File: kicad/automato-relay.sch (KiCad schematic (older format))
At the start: 51 parts, among them J1 TE-3-213598-4, J2 IEC-C14-FUSE, J3 TE-3-213598-4, J4 Screw_Terminal_01x05, J5 TE-3-213598-4, J6 TE-3-213598-4, J7 Screw_Terminal_01x05, J8 TE-3-213598-4, K1 G5LE-14, K2 G5LE-14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

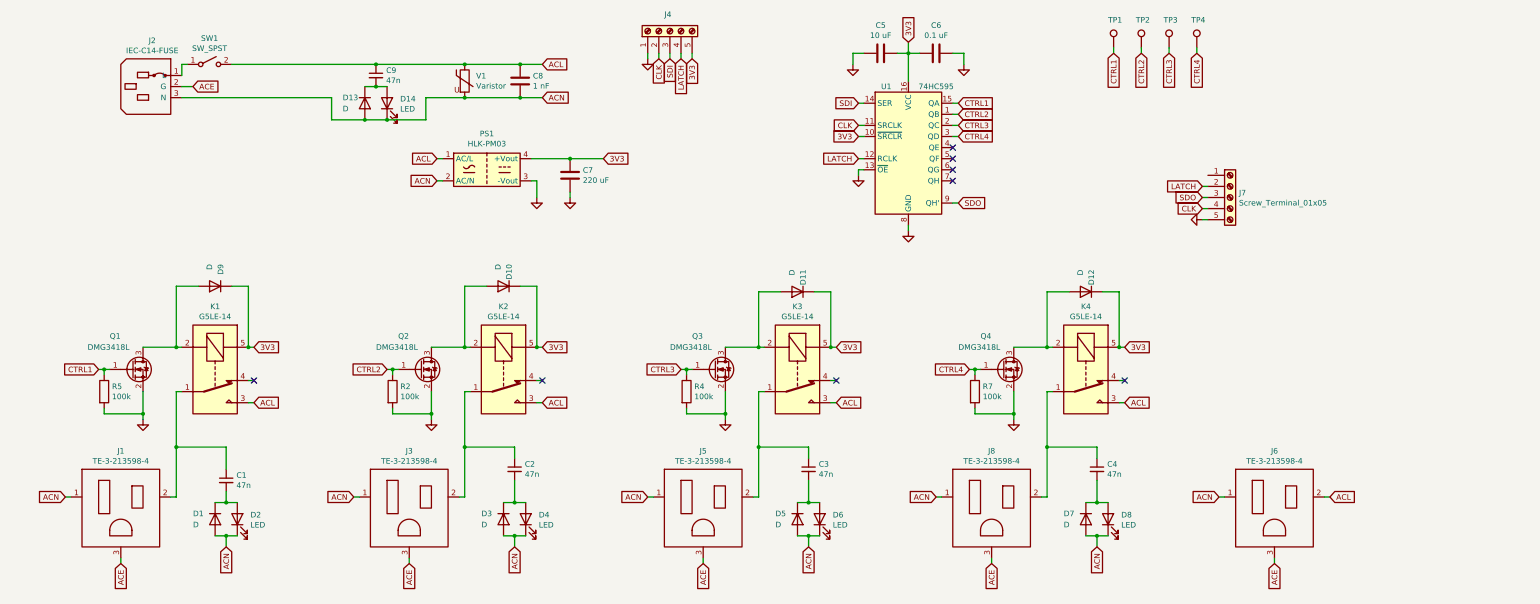
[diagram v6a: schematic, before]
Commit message: replaced 5-pin connectors with usb-c receptacles
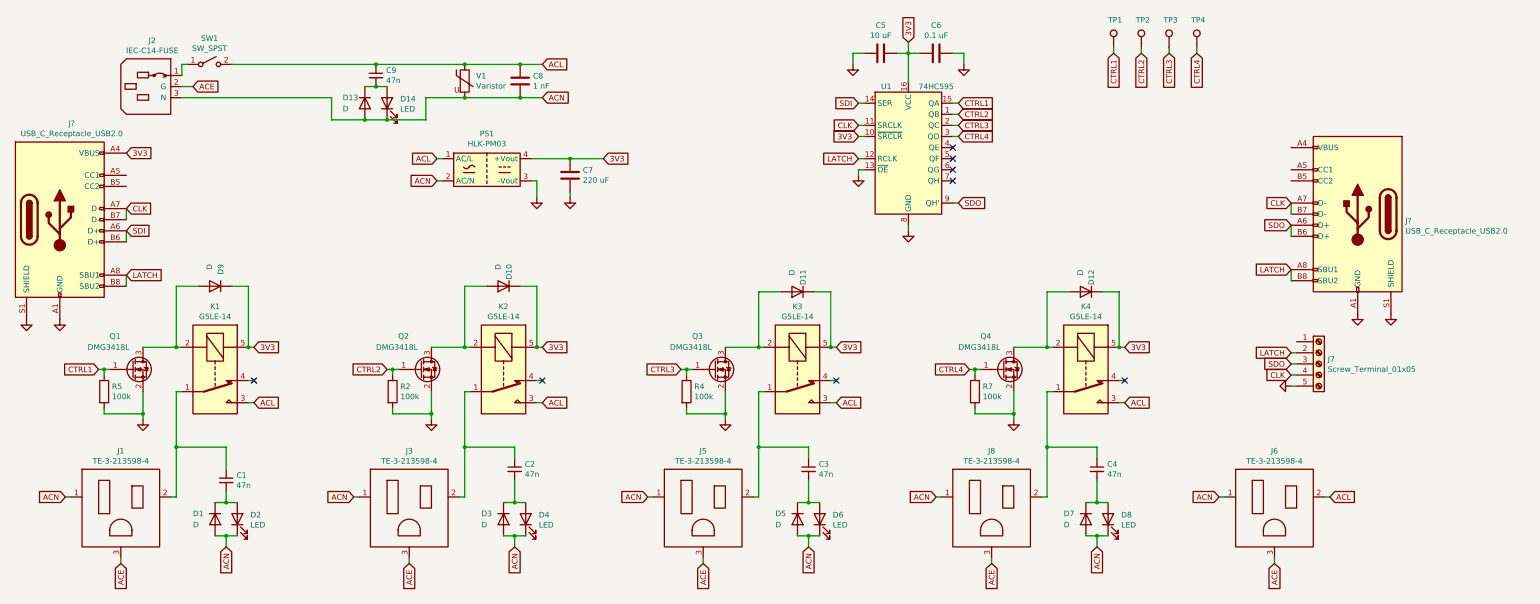
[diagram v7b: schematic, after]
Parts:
- removed J4: Screw_Terminal_01x05, automato-relay:PhoenixContact_1935190_1x5, symbol Connector:Screw_Terminal_01x05
- added J? (x2): USB_C_Receptacle_USB2.0, symbol Connector:USB_C_Receptacle_USB2.0
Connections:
- net 3V3: now also J?.A4 (VBUS), J?.A9 (VBUS), J?.B4 (VBUS), J?.B9 (VBUS)
- net CLK: now also J?.A7 (D-), J?.A7 (D-), J?.B7 (D-), J?.B7 (D-)
- net GND: now also J?.A1 (GND), J?.A1 (GND), J?.A12 (GND), J?.A12 (GND), J?.B1 (GND), J?.B1 (GND), J?.B12 (GND), J?.B12 (GND), J?.S1 (SHIELD), J?.S1 (SHIELD)
- net LATCH: now also J?.A8 (SBU1), J?.A8 (SBU1), J?.B8 (SBU2), J?.B8 (SBU2)
- net SDI: now also J?.A6 (D+), J?.B6 (D+)
- net SDO: now also J?.A6 (D+), J?.B6 (D+)
- new net: J?.A4 (VBUS), J?.A9 (VBUS), J?.B4 (VBUS), J?.B9 (VBUS)
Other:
- moved on the sheet: J7
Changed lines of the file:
@@
 	8300 2200 8350 2200
-$Comp
-L power:GND #PWR06
-U 1 1 601F84F8
-P 6400 1300
-F 0 "#PWR06" H 6400 1050 50  0001 C CNN
-F 1 "GND" H 6405 1127 50  0001 C CNN
-F 2 "" H 6400 1300 50  0001 C CNN
-F 3 "" H 6400 1300 50  0001 C CNN
-	1    6400 1300
-	1    0    0    -1
-$EndComp
-Wire Wire Line
-	6400 1250 6400 1300
-Wire Wire Line
-	6500 1250 6500 1300
-Wire Wire Line
-	6600 1250 6600 1300
-Wire Wire Line
-	6700 1250 6700 1300
 $Comp
 L power:GND #PWR012
 U 1 1 60208E2A
-P 11400 2750
-F 0 "#PWR012" H 11400 2500 50  0001 C CNN
-F 1 "GND" H 11405 2577 50  0001 C CNN
-F 2 "" H 11400 2750 50  0001 C CNN
-F 3 "" H 11400 2750 50  0001 C CNN
-	1    11400 2750
+P 12200 4250
+F 0 "#PWR012" H 12200 4000 50  0001 C CNN
+F 1 "GND" H 12205 4077 50  0001 C CNN
+F 2 "" H 12200 4250 50  0001 C CNN
+F 3 "" H 12200 4250 50  0001 C CNN
+	1    12200 4250
 	0    1    1    0
 $EndComp
-Text GLabel 6500 1300 3    50   Input ~ 0
+Text GLabel 12200 4150 0    50   Input ~ 0
 CLK
-Text GLabel 6600 1300 3    50   Input ~ 0
-SDI
-Text GLabel 6700 1300 3    50   Input ~ 0
+Text GLabel 12200 3950 0    50   Input ~ 0
 LATCH
-Text GLabel 11400 2650 0    50   Input ~ 0
-CLK
-Text GLabel 11400 2450 0    50   Input ~ 0
-LATCH
-Wire Wire Line
-	11450 2450 11400 2450
-Wire Wire Line
-	11400 2650 11450 2650
-Wire Wire Line
-	11400 2750 11450 2750
+Wire Wire Line
+	12250 3950 12200 3950
+Wire Wire Line
+	12200 4150 12250 4150
+Wire Wire Line
+	12200 4250 12250 4250
 Text GLabel 9200 2600 2    50   Input ~ 0
 SDO
 Wire Wire Line
 	9150 2600 9200 2600
-Text GLabel 11400 2550 0    50   Input ~ 0
+Text GLabel 12200 4050 0    50   Input ~ 0
 SDO
 Wire Wire Line
-	11450 2550 11400 2550
-$Comp
-L Connector:Screw_Terminal_01x05 J4
-U 1 1 602358DE
-P 6600 1050
-F 0 "J4" V 6750 1100 50  0000 R CNN
-F 1 "Screw_Terminal_01x05" V 6750 1400 50  0001 R CNN
-F 2 "automato-relay:PhoenixContact_1935190_1x5" H 6600 1050 50  0001 C CNN
-F 3 "~" H 6600 1050 50  0001 C CNN
-	1    6600 1050
-	0    -1   -1   0
-$EndComp
-Text GLabel 6800 1300 3    50   Input ~ 0
-3V3
-Wire Wire Line
-	6800 1250 6800 1300
+	12250 4050 12200 4050
 Text GLabel 8300 2000 0    50   Input ~ 0
 3V3
@@
 L Connector:Screw_Terminal_01x05 J7
 U 1 1 603D90C3
-P 11650 2550
-F 0 "J7" H 11730 2592 50  0000 L CNN
-F 1 "Screw_Terminal_01x05" H 11730 2501 50  0000 L CNN
-F 2 "automato-relay:PhoenixContact_1935190_1x5" H 11650 2550 50  0001 C CNN
-F 3 "~" H 11650 2550 50  0001 C CNN
-	1    11650 2550
+P 12450 4050
+F 0 "J7" H 12530 4092 50  0000 L CNN
+F 1 "Screw_Terminal_01x05" H 12530 4001 50  0000 L CNN
+F 2 "automato-relay:PhoenixContact_1935190_1x5" H 12450 4050 50  0001 C CNN
+F 3 "~" H 12450 4050 50  0001 C CNN
+	1    12450 4050
 	1    0    0    -1
 $EndComp
@@
 	1    0    0    -1
 $EndComp
+$Comp
+L Connector:USB_C_Receptacle_USB2.0 J?
+U 1 1 622AE17B
+P 1100 2750
+F 0 "J?" H 1207 3617 50  0000 C CNN
+F 1 "USB_C_Receptacle_USB2.0" H 1207 3526 50  0000 C CNN
+F 2 "" H 1250 2750 50  0001 C CNN
+F 3 "https://www.usb.org/sites/default/files/documents/usb_type-c.zip" H 1250 2750 50  0001 C CNN
+	1    1100 2750
+	1    0    0    -1
+$EndComp
+$Comp
+L Connector:USB_C_Receptacle_USB2.0 J?
+U 1 1 622B08FA
+P 12800 2700
+F 0 "J?" H 12370 2639 50  0000 R CNN
+F 1 "USB_C_Receptacle_USB2.0" H 12370 2548 50  0000 R CNN
+F 2 "" H 12950 2700 50  0001 C CNN
+F 3 "https://www.usb.org/sites/default/files/documents/usb_type-c.zip" H 12950 2700 50  0001 C CNN
+	1    12800 2700
+	-1   0    0    -1
+$EndComp
+$Comp
+L power:GND #PWR?
+U 1 1 622E300C
+P 1100 3650
+F 0 "#PWR?" H 1100 3400 50  0001 C CNN
+F 1 "GND" H 1105 3477 50  0001 C CNN
+F 2 "" H 1100 3650 50  0001 C CNN
+F 3 "" H 1100 3650 50  0001 C CNN
+	1    1100 3650
+	1    0    0    -1
+$EndComp
+$Comp
+L power:GND #PWR?
+U 1 1 622E354D
+P 800 3650
+F 0 "#PWR?" H 800 3400 50  0001 C CNN
+F 1 "GND" H 805 3477 50  0001 C CNN
+F 2 "" H 800 3650 50  0001 C CNN
+F 3 "" H 800 3650 50  0001 C CNN
+	1    800  3650
+	1    0    0    -1
+$EndComp
+Text GLabel 1700 2150 2    50   Input ~ 0
+3V3
+Text GLabel 1700 3250 2    50   Input ~ 0
+LATCH
+Text GLabel 1700 2650 2    50   Input ~ 0
+CLK
+Text GLabel 1700 2850 2    50   Input ~ 0
+SDI
+Wire Wire Line
+	1700 2650 1700 2750
+Wire Wire Line
+	1700 2850 1700 2950
+Wire Wire Line
+	1700 3250 1700 3350
+$Comp
+L power:GND #PWR?
+U 1 1 6231482E
+P 12800 3600
+F 0 "#PWR?" H 12800 3350 50  0001 C CNN
+F 1 "GND" H 12805 3427 50  0001 C CNN
+F 2 "" H 12800 3600 50  0001 C CNN
+F 3 "" H 12800 3600 50  0001 C CNN
+	1    12800 3600
+	1    0    0    -1
+$EndComp
+$Comp
+L power:GND #PWR?
+U 1 1 62314C83
+P 13100 3600
+F 0 "#PWR?" H 13100 3350 50  0001 C CNN
+F 1 "GND" H 13105 3427 50  0001 C CNN
+F 2 "" H 13100 3600 50  0001 C CNN
+F 3 "" H 13100 3600 50  0001 C CNN
+	1    13100 3600
+	1    0    0    -1
+$EndComp
+Text GLabel 12200 2600 0    50   Input ~ 0
+CLK
+Text GLabel 12200 2800 0    50   Input ~ 0
+SDO
+Text GLabel 12200 3200 0    50   Input ~ 0
+LATCH
+Wire Wire Line
+	12200 3200 12200 3300
+Wire Wire Line
+	12200 2800 12200 2900
+Wire Wire Line
+	12200 2600 12200 2700
 $EndSCHEMATC

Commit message: replaced screw terminals with usb-C
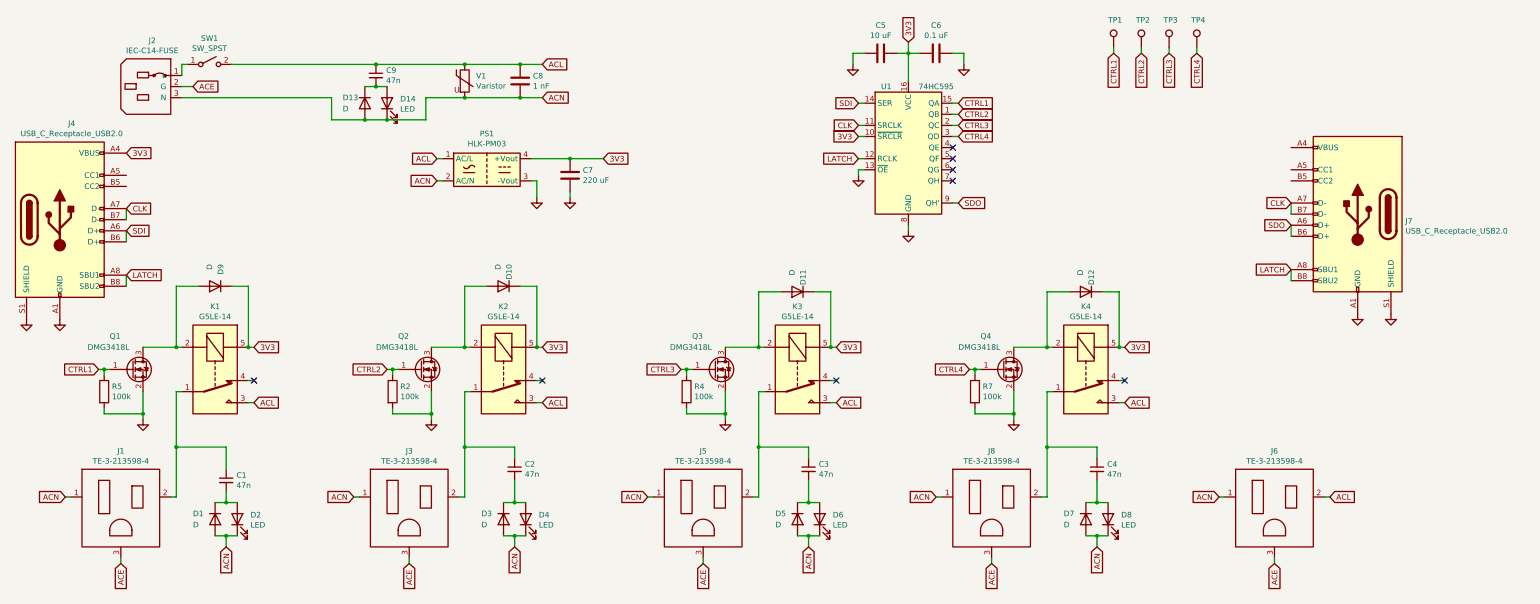
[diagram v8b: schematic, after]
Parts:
- removed J7: Screw_Terminal_01x05, automato-relay:PhoenixContact_1935190_1x5, symbol Connector:Screw_Terminal_01x05
- J4, J7: renamed from J?; footprint (none) -> automato-relay:USB_C_Receptacle_GCT-USB4105
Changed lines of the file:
@@
 Wire Wire Line
 	8300 2200 8350 2200
-$Comp
-L power:GND #PWR012
-U 1 1 60208E2A
-P 12200 4250
-F 0 "#PWR012" H 12200 4000 50  0001 C CNN
-F 1 "GND" H 12205 4077 50  0001 C CNN
-F 2 "" H 12200 4250 50  0001 C CNN
-F 3 "" H 12200 4250 50  0001 C CNN
-	1    12200 4250
-	0    1    1    0
-$EndComp
-Text GLabel 12200 4150 0    50   Input ~ 0
-CLK
-Text GLabel 12200 3950 0    50   Input ~ 0
-LATCH
-Wire Wire Line
-	12250 3950 12200 3950
-Wire Wire Line
-	12200 4150 12250 4150
-Wire Wire Line
-	12200 4250 12250 4250
 Text GLabel 9200 2600 2    50   Input ~ 0
 SDO
 Wire Wire Line
 	9150 2600 9200 2600
-Text GLabel 12200 4050 0    50   Input ~ 0
-SDO
-Wire Wire Line
-	12250 4050 12200 4050
 Text GLabel 8300 2000 0    50   Input ~ 0
 3V3
@@
 	2150 3900 2200 3900
 $Comp
-L Connector:Screw_Terminal_01x05 J7
-U 1 1 603D90C3
-P 12450 4050
-F 0 "J7" H 12530 4092 50  0000 L CNN
-F 1 "Screw_Terminal_01x05" H 12530 4001 50  0000 L CNN
-F 2 "automato-relay:PhoenixContact_1935190_1x5" H 12450 4050 50  0001 C CNN
-F 3 "~" H 12450 4050 50  0001 C CNN
-	1    12450 4050
-	1    0    0    -1
-$EndComp
-$Comp
 L Device:Varistor V1
 U 1 1 60401D0D
@@
 $EndComp
 $Comp
-L Connector:USB_C_Receptacle_USB2.0 J?
+L Connector:USB_C_Receptacle_USB2.0 J4
 U 1 1 622AE17B
 P 1100 2750
-F 0 "J?" H 1207 3617 50  0000 C CNN
+F 0 "J4" H 1207 3617 50  0000 C CNN
 F 1 "USB_C_Receptacle_USB2.0" H 1207 3526 50  0000 C CNN
-F 2 "" H 1250 2750 50  0001 C CNN
+F 2 "automato-relay:USB_C_Receptacle_GCT-USB4105" H 1250 2750 50  0001 C CNN
 F 3 "https://www.usb.org/sites/default/files/documents/usb_type-c.zip" H 1250 2750 50  0001 C CNN
 	1    1100 2750
@@
 $EndComp
 $Comp
-L Connector:USB_C_Receptacle_USB2.0 J?
+L Connector:USB_C_Receptacle_USB2.0 J7
 U 1 1 622B08FA
 P 12800 2700
-F 0 "J?" H 12370 2639 50  0000 R CNN
+F 0 "J7" H 12370 2639 50  0000 R CNN
 F 1 "USB_C_Receptacle_USB2.0" H 12370 2548 50  0000 R CNN
-F 2 "" H 12950 2700 50  0001 C CNN
+F 2 "automato-relay:USB_C_Receptacle_GCT-USB4105" H 12950 2700 50  0001 C CNN
 F 3 "https://www.usb.org/sites/default/files/documents/usb_type-c.zip" H 12950 2700 50  0001 C CNN
 	1    12800 2700
@@
 $EndComp
 $Comp
-L power:GND #PWR?
+L power:GND #PWR0101
 U 1 1 622E300C
 P 1100 3650
-F 0 "#PWR?" H 1100 3400 50  0001 C CNN
+F 0 "#PWR0101" H 1100 3400 50  0001 C CNN
 F 1 "GND" H 1105 3477 50  0001 C CNN
 F 2 "" H 1100 3650 50  0001 C CNN
@@
 $EndComp
 $Comp
-L power:GND #PWR?
+L power:GND #PWR0102
 U 1 1 622E354D
 P 800 3650
-F 0 "#PWR?" H 800 3400 50  0001 C CNN
+F 0 "#PWR0102" H 800 3400 50  0001 C CNN
 F 1 "GND" H 805 3477 50  0001 C CNN
 F 2 "" H 800 3650 50  0001 C CNN
@@
 	1700 3250 1700 3350
 $Comp
-L power:GND #PWR?
+L power:GND #PWR0103
 U 1 1 6231482E
 P 12800 3600
-F 0 "#PWR?" H 12800 3350 50  0001 C CNN
+F 0 "#PWR0103" H 12800 3350 50  0001 C CNN
 F 1 "GND" H 12805 3427 50  0001 C CNN
 F 2 "" H 12800 3600 50  0001 C CNN
@@
 $EndComp
 $Comp
-L power:GND #PWR?
+L power:GND #PWR0104
 U 1 1 62314C83
 P 13100 3600
-F 0 "#PWR?" H 13100 3350 50  0001 C CNN
+F 0 "#PWR0104" H 13100 3350 50  0001 C CNN
 F 1 "GND" H 13105 3427 50  0001 C CNN
 F 2 "" H 13100 3600 50  0001 C CNN
